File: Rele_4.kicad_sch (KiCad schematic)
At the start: 5 parts

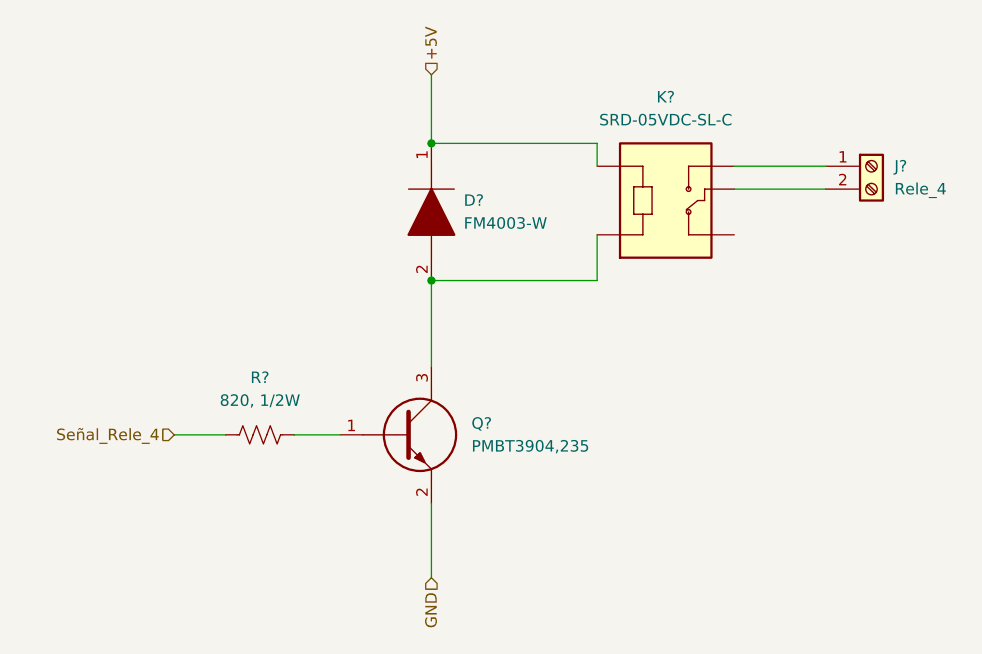
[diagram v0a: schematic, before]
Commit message: Ajuste del esquematico
Se cambio el integrado ESP32 por 2 tiras de pines de 1x15, se quitaron los switches EN y BOOT que ya estan en el NodeMCU, se quito el mutliplexor 74HC y se cablearon las I/O
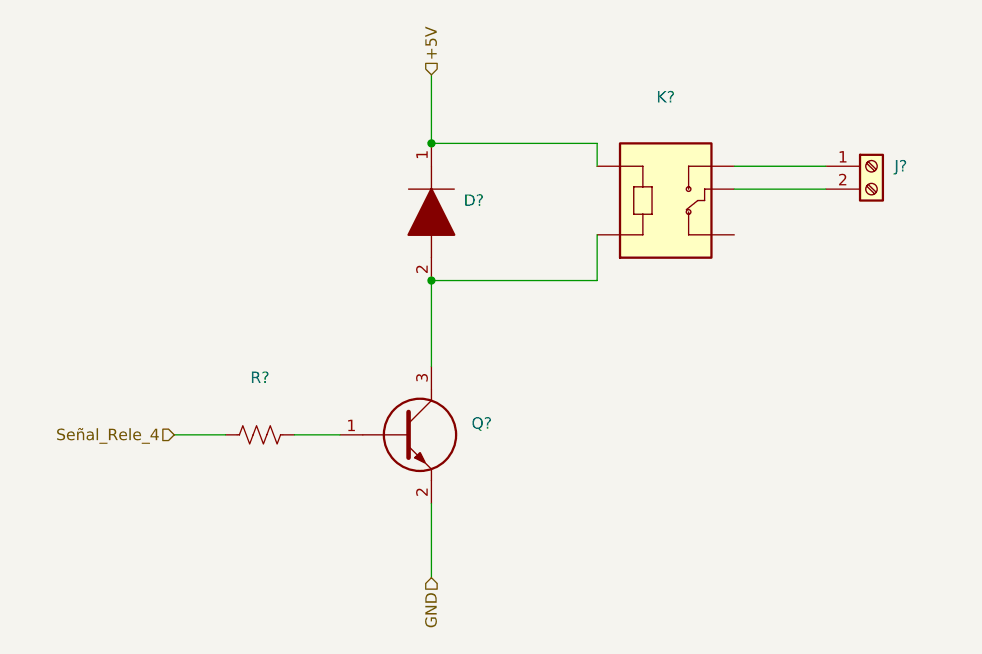
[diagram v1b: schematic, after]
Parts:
- D?: value FM4003-W -> (none); footprint DIOM5025X231N -> (none)
- J?: value Rele_4 -> (none)
- K?: value SRD-05VDC-SL-C -> (none); footprint RELAY_SRD-05VDC-SL-C -> (none)
- Q?: value PMBT3904,235 -> (none); footprint SOT95P230X110-3N -> (none)
- R?: value 820, 1/2W -> (none)
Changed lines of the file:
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@@
     (in_bom yes) (on_board yes) (fields_autoplaced)
     (property "Reference" "R?" (id 0) (at 123.825 98.425 90))
-    (property "Value" "820, 1/2W" (id 1) (at 123.825 100.965 90))
+    (property "Value" "" (id 1) (at 123.825 100.965 90))
     (property "Footprint" "" (id 2) (at 124.079 103.759 90)
       (effects (font (size 1.27 1.27)) hide)
@@
       (effects (font (size 1.27 1.27)) (justify left))
     )
-    (property "Value" "PMBT3904,235" (id 1) (at 147.32 106.0449 0)
+    (property "Value" "" (id 1) (at 147.32 106.0449 0)
       (effects (font (size 1.27 1.27)) (justify left))
     )
-    (property "Footprint" "SOT95P230X110-3N" (id 2) (at 146.685 108.585 0)
+    (property "Footprint" "" (id 2) (at 146.685 108.585 0)
       (effects (font (size 1.27 1.27)) (justify left) hide)
     )
@@
       (effects (font (size 1.27 1.27)) (justify left))
     )
-    (property "Value" "Rele_4" (id 1) (at 194.31 77.4699 0)
+    (property "Value" "" (id 1) (at 194.31 77.4699 0)
       (effects (font (size 1.27 1.27)) (justify left))
     )
@@
     (in_bom yes) (on_board yes) (fields_autoplaced)
     (property "Reference" "K?" (id 0) (at 168.91 67.2592 0))
-    (property "Value" "SRD-05VDC-SL-C" (id 1) (at 168.91 69.7992 0))
-    (property "Footprint" "RELAY_SRD-05VDC-SL-C" (id 2) (at 168.91 77.47 0)
+    (property "Value" "" (id 1) (at 168.91 69.7992 0))
+    (property "Footprint" "" (id 2) (at 168.91 77.47 0)
       (effects (font (size 1.27 1.27)) (justify left bottom) hide)
     )
@@
       (effects (font (size 1.27 1.27)) (justify left))
     )
-    (property "Value" "FM4003-W" (id 1) (at 146.4564 81.2799 90)
+    (property "Value" "" (id 1) (at 146.4564 81.2799 90)
       (effects (font (size 1.27 1.27)) (justify left))
     )
-    (property "Footprint" "DIOM5025X231N" (id 2) (at 142.875 83.82 0)
+    (property "Footprint" "" (id 2) (at 142.875 83.82 0)
       (effects (font (size 1.27 1.27)) (justify left) hide)
     )

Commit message: Modificación de posición de circ. filtrado y circ. de adaptación de tensión
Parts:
- D?, J?, K?, Q?, R?: value (none) -> ~
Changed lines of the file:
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@@
     (in_bom yes) (on_board yes) (fields_autoplaced)
     (property "Reference" "R?" (id 0) (at 123.825 98.425 90))
-    (property "Value" "" (id 1) (at 123.825 100.965 90))
+    (property "Value" "~" (id 1) (at 123.825 100.965 90))
     (property "Footprint" "" (id 2) (at 124.079 103.759 90)
       (effects (font (size 1.27 1.27)) hide)
@@
       (effects (font (size 1.27 1.27)) (justify left))
     )
-    (property "Value" "" (id 1) (at 147.32 106.0449 0)
+    (property "Value" "~" (id 1) (at 147.32 106.0449 0)
       (effects (font (size 1.27 1.27)) (justify left))
     )
@@
       (effects (font (size 1.27 1.27)) (justify left))
     )
-    (property "Value" "" (id 1) (at 194.31 77.4699 0)
+    (property "Value" "~" (id 1) (at 194.31 77.4699 0)
       (effects (font (size 1.27 1.27)) (justify left))
     )
@@
     (in_bom yes) (on_board yes) (fields_autoplaced)
     (property "Reference" "K?" (id 0) (at 168.91 67.2592 0))
-    (property "Value" "" (id 1) (at 168.91 69.7992 0))
+    (property "Value" "~" (id 1) (at 168.91 69.7992 0))
     (property "Footprint" "" (id 2) (at 168.91 77.47 0)
       (effects (font (size 1.27 1.27)) (justify left bottom) hide)
@@
       (effects (font (size 1.27 1.27)) (justify left))
     )
-    (property "Value" "" (id 1) (at 146.4564 81.2799 90)
+    (property "Value" "~" (id 1) (at 146.4564 81.2799 90)
       (effects (font (size 1.27 1.27)) (justify left))
     )

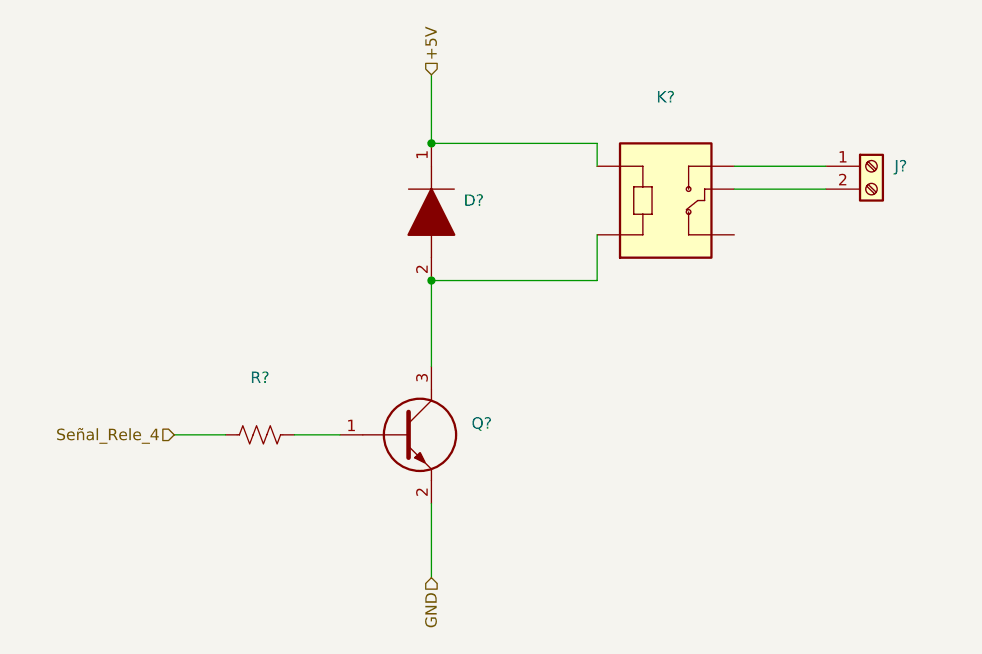
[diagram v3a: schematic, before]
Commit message: Actualización de SCH según placa industrial, y búsqueda de footprints.
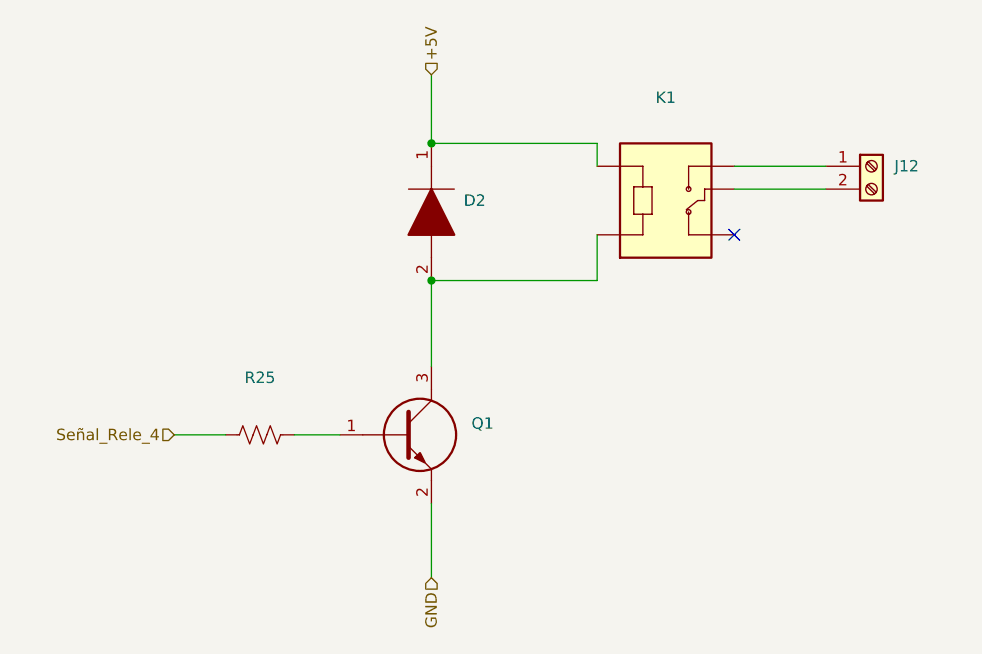
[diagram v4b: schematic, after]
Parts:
- D2: renamed from D?; value ~ -> (none)
- J12: renamed from J?; value ~ -> (none)
- K1: renamed from K?; value ~ -> (none)
- Q1: renamed from Q?; value ~ -> (none)
- R25: renamed from R?; value ~ -> (none)
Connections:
- no-connect marks 0 -> 1
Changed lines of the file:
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@@
   (junction (at 142.875 72.39) (diameter 0) (color 0 0 0 0)
   )
+  (no_connect (at 176.53 82.55))
   (wire (pts (xy 161.29 72.39) (xy 161.29 74.93))
     (stroke (width 0) (type default) (color 0 0 0 0))
@@
   (symbol (lib_id "Device:R_US") (at 123.825 104.775 90) (unit 1)
     (in_bom yes) (on_board yes) (fields_autoplaced)
-    (property "Reference" "R?" (id 0) (at 123.825 98.425 90))
-    (property "Value" "~" (id 1) (at 123.825 100.965 90))
+    (property "Reference" "R25" (id 0) (at 123.825 98.425 90))
+    (property "Value" "" (id 1) (at 123.825 100.965 90))
     (property "Footprint" "" (id 2) (at 124.079 103.759 90)
       (effects (font (size 1.27 1.27)) hide)
@@
   (symbol (lib_id "PMBT3904,235:PMBT3904,235") (at 132.715 104.775 0) (unit 1)
     (in_bom yes) (on_board yes) (fields_autoplaced)
-    (property "Reference" "Q?" (id 0) (at 147.32 103.5049 0)
+    (property "Reference" "Q1" (id 0) (at 147.32 103.5049 0)
       (effects (font (size 1.27 1.27)) (justify left))
     )
-    (property "Value" "~" (id 1) (at 147.32 106.0449 0)
+    (property "Value" "" (id 1) (at 147.32 106.0449 0)
       (effects (font (size 1.27 1.27)) (justify left))
     )
@@
   (symbol (lib_id "Connector:Screw_Terminal_01x02") (at 191.77 74.93 0) (unit 1)
     (in_bom yes) (on_board yes) (fields_autoplaced)
-    (property "Reference" "J?" (id 0) (at 194.31 74.9299 0)
+    (property "Reference" "J12" (id 0) (at 194.31 74.9299 0)
       (effects (font (size 1.27 1.27)) (justify left))
     )
-    (property "Value" "~" (id 1) (at 194.31 77.4699 0)
+    (property "Value" "" (id 1) (at 194.31 77.4699 0)
       (effects (font (size 1.27 1.27)) (justify left))
     )
@@
   (symbol (lib_id "SRD-05VDC-SL-C:SRD-05VDC-SL-C") (at 168.91 77.47 0) (unit 1)
     (in_bom yes) (on_board yes) (fields_autoplaced)
-    (property "Reference" "K?" (id 0) (at 168.91 67.2592 0))
-    (property "Value" "~" (id 1) (at 168.91 69.7992 0))
+    (property "Reference" "K1" (id 0) (at 168.91 67.31 0))
+    (property "Value" "" (id 1) (at 168.91 69.85 0))
     (property "Footprint" "" (id 2) (at 168.91 77.47 0)
       (effects (font (size 1.27 1.27)) (justify left bottom) hide)
@@
   (symbol (lib_id "FM4003-W:FM4003-W") (at 142.875 72.39 270) (unit 1)
     (in_bom yes) (on_board yes) (fields_autoplaced)
-    (property "Reference" "D?" (id 0) (at 146.4564 78.7399 90)
+    (property "Reference" "D2" (id 0) (at 146.4564 78.7399 90)
       (effects (font (size 1.27 1.27)) (justify left))
     )
-    (property "Value" "~" (id 1) (at 146.4564 81.2799 90)
+    (property "Value" "" (id 1) (at 146.4564 81.2799 90)
       (effects (font (size 1.27 1.27)) (justify left))
     )

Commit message: Fin de SCH, config de inicio para PCB
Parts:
- D2: value (none) -> FM4003-W; footprint (none) -> FM4003W:DIOM5025X231N
- J12: value (none) -> Rele_4; footprint (none) -> TB002-500-02BE:TB00250002BE
- K1: value (none) -> SRD-05VDC-SL-C; footprint (none) -> SRD-05VDC-SL-C-Version_2:RELAY_SRD-05VDC-SL-C
- Q1: value (none) -> PMBT3904,235; footprint (none) -> PMBT3904,235:SOT95P230X110-3N
- R25: value (none) -> 820, 1/2W; footprint (none) -> Resistor_SMD:R_0805_2012Metric
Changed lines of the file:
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@@
     (in_bom yes) (on_board yes) (fields_autoplaced)
     (property "Reference" "R25" (id 0) (at 123.825 98.425 90))
-    (property "Value" "" (id 1) (at 123.825 100.965 90))
-    (property "Footprint" "" (id 2) (at 124.079 103.759 90)
+    (property "Value" "820, 1/2W" (id 1) (at 123.825 100.965 90))
+    (property "Footprint" "Resistor_SMD:R_0805_2012Metric" (id 2) (at 124.079 103.759 90)
       (effects (font (size 1.27 1.27)) hide)
     )
@@
       (effects (font (size 1.27 1.27)) (justify left))
     )
-    (property "Value" "" (id 1) (at 147.32 106.0449 0)
+    (property "Value" "PMBT3904,235" (id 1) (at 147.32 106.0449 0)
       (effects (font (size 1.27 1.27)) (justify left))
     )
-    (property "Footprint" "" (id 2) (at 146.685 108.585 0)
+    (property "Footprint" "PMBT3904,235:SOT95P230X110-3N" (id 2) (at 146.685 108.585 0)
       (effects (font (size 1.27 1.27)) (justify left) hide)
     )
@@
       (effects (font (size 1.27 1.27)) (justify left))
     )
-    (property "Value" "" (id 1) (at 194.31 77.4699 0)
+    (property "Value" "Rele_4" (id 1) (at 194.31 77.4699 0)
       (effects (font (size 1.27 1.27)) (justify left))
     )
-    (property "Footprint" "" (id 2) (at 191.77 74.93 0)
+    (property "Footprint" "TB002-500-02BE:TB00250002BE" (id 2) (at 191.77 74.93 0)
       (effects (font (size 1.27 1.27)) hide)
     )
@@
     (in_bom yes) (on_board yes) (fields_autoplaced)
     (property "Reference" "K1" (id 0) (at 168.91 67.31 0))
-    (property "Value" "" (id 1) (at 168.91 69.85 0))
-    (property "Footprint" "" (id 2) (at 168.91 77.47 0)
+    (property "Value" "SRD-05VDC-SL-C" (id 1) (at 168.91 69.85 0))
+    (property "Footprint" "SRD-05VDC-SL-C-Version_2:RELAY_SRD-05VDC-SL-C" (id 2) (at 168.91 77.47 0)
       (effects (font (size 1.27 1.27)) (justify left bottom) hide)
     )
@@
       (effects (font (size 1.27 1.27)) (justify left))
     )
-    (property "Value" "" (id 1) (at 146.4564 81.2799 90)
+    (property "Value" "FM4003-W" (id 1) (at 146.4564 81.2799 90)
       (effects (font (size 1.27 1.27)) (justify left))
     )
-    (property "Footprint" "" (id 2) (at 142.875 83.82 0)
+    (property "Footprint" "FM4003W:DIOM5025X231N" (id 2) (at 142.875 83.82 0)
       (effects (font (size 1.27 1.27)) (justify left) hide)
     )

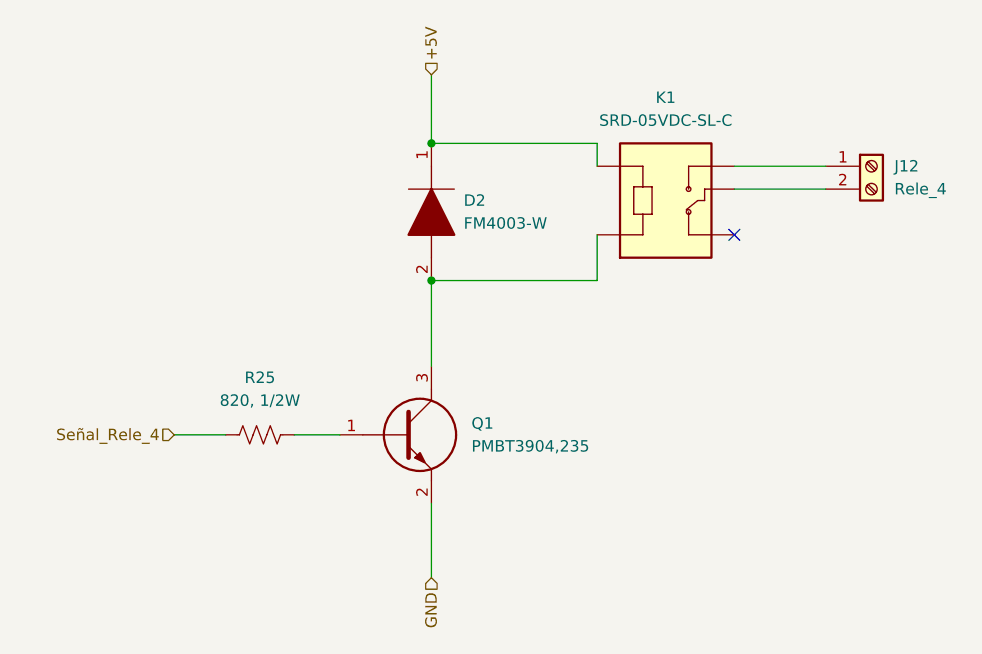
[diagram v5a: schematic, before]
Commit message: Cambios en SCH y PCB.
Se cambio el adaptador de nivel 5-3,3V por un circuito con MOSFET 2N7002, dado que ya no hay stock del NXB. Se modificó el footprint del expansor I/O por uno thorugh-hole.
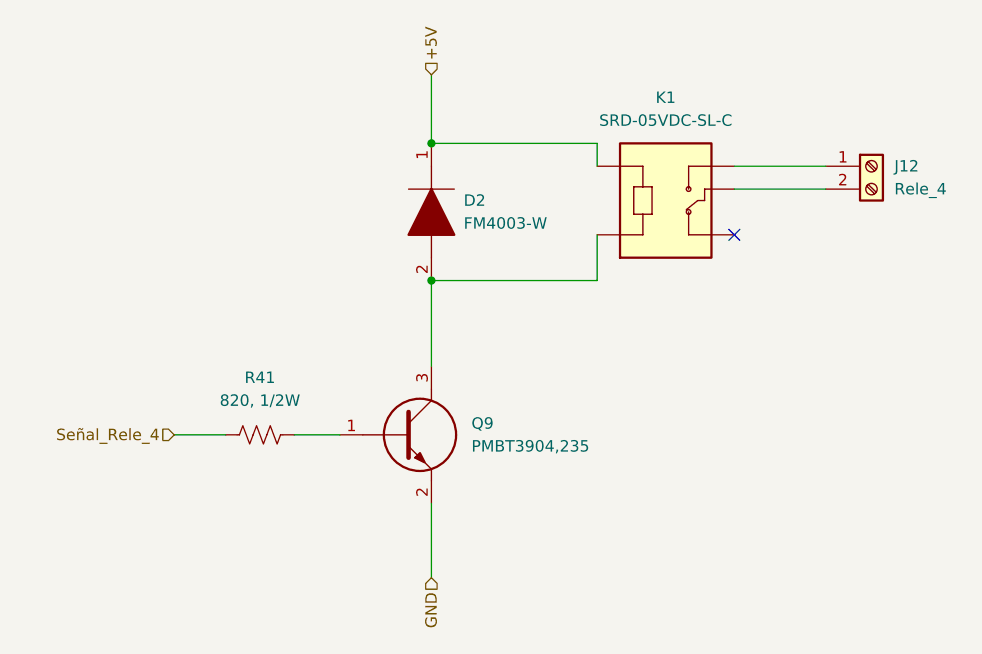
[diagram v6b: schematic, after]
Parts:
- renumbered Q1 to Q9, R25 to R41
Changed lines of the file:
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@@
   (symbol (lib_id "Device:R_US") (at 123.825 104.775 90) (unit 1)
     (in_bom yes) (on_board yes) (fields_autoplaced)
-    (property "Reference" "R25" (id 0) (at 123.825 98.425 90))
+    (property "Reference" "R41" (id 0) (at 123.825 98.425 90))
     (property "Value" "820, 1/2W" (id 1) (at 123.825 100.965 90))
     (property "Footprint" "Resistor_SMD:R_0805_2012Metric" (id 2) (at 124.079 103.759 90)
@@
   (symbol (lib_id "PMBT3904,235:PMBT3904,235") (at 132.715 104.775 0) (unit 1)
     (in_bom yes) (on_board yes) (fields_autoplaced)
-    (property "Reference" "Q1" (id 0) (at 147.32 103.5049 0)
+    (property "Reference" "Q9" (id 0) (at 147.32 103.5049 0)
       (effects (font (size 1.27 1.27)) (justify left))
     )

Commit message: Se finalizó con el PCB del prototipo.
Dado que se buscó a toda costa que el PCB fuera de 1 capa, en varios puntos del circuito se tuvieron que agregar pin headers individuales para conectar a 3V3 y GND, junto con tiras de pin headers. Cada una de estas se conectara luego entre si mediante cables.

Tambien se generaron los archivos Gerber y BOM.
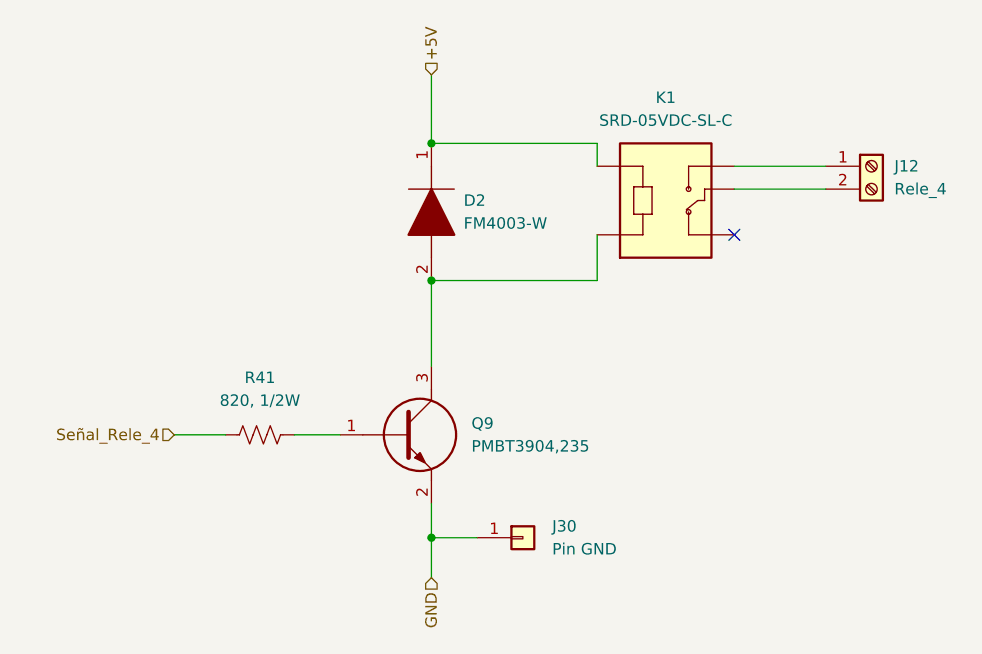
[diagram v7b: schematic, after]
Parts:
- added J30: Pin GND, Connector_PinHeader_2.54mm:PinHeader_1x01_P2.54mm_Vertical, symbol Connector_Generic:Conn_01x01
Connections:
- net GND: now also J30.1 (Pin_1)
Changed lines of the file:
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@@
 (kicad_sch (version 20211123) (generator eeschema)
   (paper "A4")
+  (junction (at 142.875 116.205) (diameter 0) (color 0 0 0 0)
+  )
   (junction (at 142.875 87.63) (diameter 0) (color 0 0 0 0)
   )
@@
     (stroke (width 0) (type default) (color 0 0 0 0))
   )
+  (wire (pts (xy 142.875 116.205) (xy 142.875 120.65))
+    (stroke (width 0) (type default) (color 0 0 0 0))
+  )
   (wire (pts (xy 142.875 72.39) (xy 161.29 72.39))
     (stroke (width 0) (type default) (color 0 0 0 0))
@@
     (stroke (width 0) (type default) (color 0 0 0 0))
   )
-  (wire (pts (xy 142.875 112.395) (xy 142.875 120.65))
+  (wire (pts (xy 142.875 112.395) (xy 142.875 116.205))
     (stroke (width 0) (type default) (color 0 0 0 0))
   )
@@
   )
   (wire (pts (xy 142.875 87.63) (xy 161.29 87.63))
+    (stroke (width 0) (type default) (color 0 0 0 0))
+  )
+  (wire (pts (xy 142.875 116.205) (xy 147.955 116.205))
     (stroke (width 0) (type default) (color 0 0 0 0))
   )
@@
     (effects (font (size 1.27 1.27)) (justify right))
   )
+  (symbol (lib_id "Connector_Generic:Conn_01x01") (at 153.035 116.205 0) (unit 1)
+    (in_bom yes) (on_board yes) (fields_autoplaced)
+    (property "Reference" "J30" (id 0) (at 156.2862 114.9349 0)
+      (effects (font (size 1.27 1.27)) (justify left))
+    )
+    (property "Value" "Pin GND" (id 1) (at 156.2862 117.4749 0)
+      (effects (font (size 1.27 1.27)) (justify left))
+    )
+    (property "Footprint" "Connector_PinHeader_2.54mm:PinHeader_1x01_P2.54mm_Vertical" (id 2) (at 153.035 116.205 0)
+      (effects (font (size 1.27 1.27)) hide)
+    )
+    (property "Datasheet" "~" (id 3) (at 153.035 116.205 0)
+      (effects (font (size 1.27 1.27)) hide)
+    )
+    (pin "1")
+  )
   (symbol (lib_id "Device:R_US") (at 123.825 104.775 90) (unit 1)
